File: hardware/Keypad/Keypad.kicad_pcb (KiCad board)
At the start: 2 copper layers, 13.1 x 26.7 mm, 7 parts, among them J5 Keypad1, SW3 RIGHT, SW4 LEFT, SW5 SET

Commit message: redesign pcb files
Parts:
- removed J5: Keypad1, Connector_PinHeader_2.54mm:PinHeader_1x05_P2.54mm_Vertical
- removed R6, R7, R8: 10k, Resistor_SMD:R_1206_3216Metric_Pad1.30x1.75mm_HandSolder
- removed SW4: LEFT, Button_Switch_SMD:SW_SPST_FSMSM
- removed SW5: SET, Button_Switch_SMD:SW_SPST_FSMSM
- added Brd1: SSD1306, SSD1306:128x64OLED, F.Cu at (39.1, 88.6)
- added H4: MountingHole, MountingHole:MountingHole_2.2mm_M2, F.Cu at (25.3, 77.5)
- added H5: MountingHole, MountingHole:MountingHole_2.2mm_M2, F.Cu at (25.3, 99.1)
- added H6: MountingHole, MountingHole:MountingHole_2.2mm_M2, F.Cu at (56.2, 77.5)
- added H7: MountingHole, MountingHole:MountingHole_2.2mm_M2, F.Cu at (56.2, 99.1)
- added J1: Keypad1, Connector_PinHeader_2.54mm:PinHeader_1x05_P2.54mm_Vertical, B.Cu at (52.8, 83.2)
- added J2: LCD, Connector_PinHeader_2.54mm:PinHeader_1x04_P2.54mm_Vertical, B.Cu at (25.0, 92.3)
- added R1: 10k, Resistor_SMD:R_1206_3216Metric_Pad1.30x1.75mm_HandSolder, F.Cu at (48.5, 88.3)
- added R2: 10k, Resistor_SMD:R_1206_3216Metric_Pad1.30x1.75mm_HandSolder, F.Cu at (48.5, 85.7)
- added R3: 10k, Resistor_SMD:R_1206_3216Metric_Pad1.30x1.75mm_HandSolder, F.Cu at (48.5, 90.8)
- added SW1: LEFT, Button_Switch_SMD:SW_SPST_FSMSM, F.Cu at (60.9, 94.4)
- added SW2: RIGHT, Button_Switch_SMD:SW_SPST_FSMSM, F.Cu at (60.9, 82.1)
- SW3: value RIGHT -> SET
- moved SW3 7.40 mm to (56.7, 88.3)
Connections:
- SW3 pad 1: (no net) -> GND
- SW3 pad 2: (no net) -> /IO12
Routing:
- net (no net): track 72.5 -> 0.00 mm, vias 1 -> 0
- net +3V3: track 0.00 -> 38.2 mm
- net /IO14: track 0.00 -> 17.1 mm
- net /IO13: track 0.00 -> 11.3 mm
- net /IO12: track 0.00 -> 7.55 mm
- net /SDA: track 0.00 -> 4.12 mm
- net /SCK: track 0.00 -> 4.12 mm
- added copper zone on B.Cu, net GND
- added copper zone on F.Cu, net GND
- removed copper zone on B.Cu, net (none)
- removed copper zone on F.Cu, net (none)
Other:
- board size 13.1 x 26.7 mm -> 41.1 x 26.7 mm

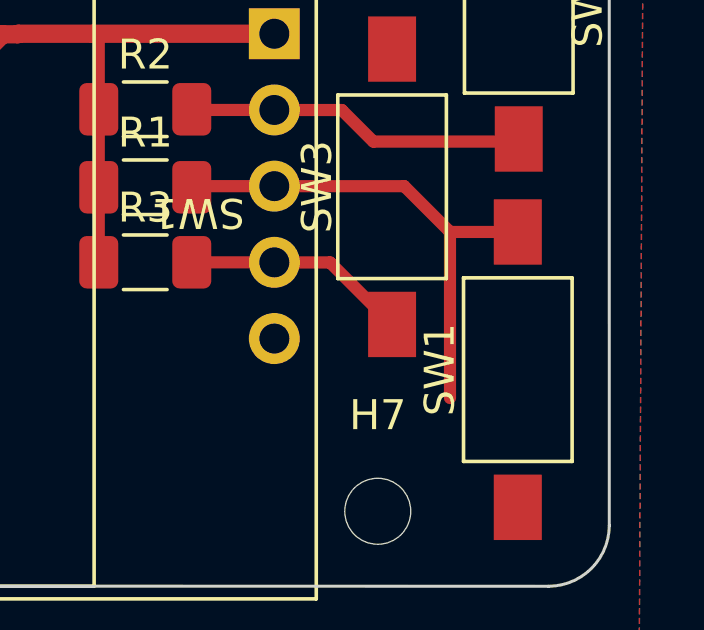
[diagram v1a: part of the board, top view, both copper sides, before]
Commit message: minor change on keypad
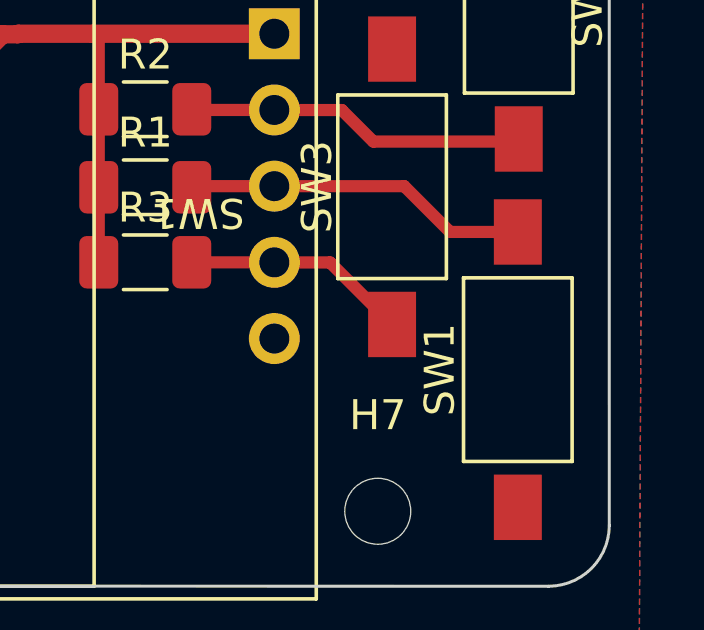
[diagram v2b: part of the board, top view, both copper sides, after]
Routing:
- net /IO14: track 17.1 -> 11.5 mm
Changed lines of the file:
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@@
-	)
-	(segment
-		(start 58.607951 95.3262)
-		(end 58.607951 89.789)
-		(width 0.4064)
-		(layer "F.Cu")
-		(net 5)
 	)
 	(segment
